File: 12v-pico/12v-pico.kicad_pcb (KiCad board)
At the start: 2 copper layers, 75 x 68 mm, 13 parts, among them J1 MERG 12v CBUS, J2 Adafruit CAN Pal, J3 UART0, J4 DEBUG, J5 Conn_01x20_Pin, J6 Conn_01x20_Pin, SW1 RESET, U1 LM7805_TO220

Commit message: tidied up schematic
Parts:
- renumbered J4 to J3, J3 to J4
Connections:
- net +12V renamed Net-(D1-A)
- SW1 pad 1: Net-(A1-RUN) -> GND
- SW1 pad 2: GND -> Net-(A1-RUN)
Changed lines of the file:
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@@
 	(net 35 "Net-(A1-GPIO0)")
 	(net 36 "Net-(A1-GPIO6)")
-	(net 37 "+12V")
+	(net 37 "Net-(D1-A)")
 	(net 38 "Net-(D1-K)")
 	(net 39 "Net-(D2-A)")
@@
 			(remove_unused_layers no)
 			(net 14 "Net-(A1-VBUS)")
-			(pinfunction "Pin_1")
+			(pinfunction "40")
 			(pintype "passive")
 		)
@@
 		(descr "Through hole straight socket strip, 1x03, 2.54mm pitch, single row (from Kicad 4.0.7), script generated")
 		(tags "Through hole socket strip THT 1x03 2.54mm single row")
-		(property "Reference" "J3"
+		(property "Reference" "J4"
 			(at -3.24 -0.338 0)
 			(layer "F.SilkS")
@@
 			(layers "*.Cu" "*.Mask")
 			(remove_unused_layers no)
-			(net 3 "Net-(A1-RUN)")
+			(net 7 "GND")
 			(pinfunction "1")
 			(pintype "passive")
@@
 			(layers "*.Cu" "*.Mask")
 			(remove_unused_layers no)
-			(net 3 "Net-(A1-RUN)")
+			(net 7 "GND")
 			(pinfunction "1")
 			(pintype "passive")
@@
 			(layers "*.Cu" "*.Mask")
 			(remove_unused_layers no)
-			(net 7 "GND")
+			(net 3 "Net-(A1-RUN)")
 			(pinfunction "2")
 			(pintype "passive")
@@
 			(layers "*.Cu" "*.Mask")
 			(remove_unused_layers no)
-			(net 7 "GND")
+			(net 3 "Net-(A1-RUN)")
 			(pinfunction "2")
 			(pintype "passive")
@@
 			(layers "*.Cu" "*.Mask")
 			(remove_unused_layers no)
-			(net 37 "+12V")
+			(net 37 "Net-(D1-A)")
 			(pinfunction "A")
 			(pintype "passive")
@@
 		(descr "Through hole straight pin header, 1x03, 2.54mm pitch, single row")
 		(tags "Through hole pin header THT 1x03 2.54mm single row")
-		(property "Reference" "J4"
+		(property "Reference" "J3"
 			(at 0 -2.38 90)
 			(layer "F.SilkS")
@@
 			(remove_unused_layers no)
 			(roundrect_rratio 0.104167)
-			(net 37 "+12V")
-			(pinfunction "12v")
+			(net 37 "Net-(D1-A)")
+			(pinfunction "+12v")
 			(pintype "power_out")
 		)

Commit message: design updates
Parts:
- added REF**: MountingHole_3.2mm_M3_Pad, MountingHole:MountingHole_3.2mm_M3_Pad, F.Cu at (213.0, 98.0)
- added REF**: MountingHole_3.2mm_M3_Pad, MountingHole:MountingHole_3.2mm_M3_Pad, F.Cu at (141.0, 98.0)
- added REF**: MountingHole_3.2mm_M3_Pad, MountingHole:MountingHole_3.2mm_M3_Pad, F.Cu at (213.0, 40.0)
- added REF**: MountingHole_3.2mm_M3_Pad, MountingHole:MountingHole_3.2mm_M3_Pad, F.Cu at (141.0, 40.0)
- J5: value Conn_01x20_Pin -> Pico LHS
- J6: value Conn_01x20_Pin -> Pico RHS
- moved D2 29.1 mm to (213.0, 46.9), turned to -90 degrees
- moved D1 26.2 mm to (213.0, 74.1)
- moved C2 26.0 mm to (206.0, 88.5)
- moved U1 25.6 mm to (213.0, 81.0)
- moved C1 24.9 mm to (206.0, 79.0)
- moved J2 14.9 mm to (204.1, 53.0), turned to -90 degrees
- moved J4 10.7 mm to (141.0, 48.0)
- moved SW1 7.27 mm to (177.2, 98.2), turned to 180 degrees
- moved J1 1.74 mm to (201.8, 40.7)
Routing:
- net Net-(A1-GPIO3): track 50.2 -> 73.7 mm
- net Net-(A1-GPIO2): track 50.2 -> 69.7 mm
- net Net-(D1-A): track 8.75 -> 27.9 mm
- net Net-(J1-CANH): track 32.2 -> 13.7 mm
- net Net-(J1-CANL): track 36.2 -> 20.7 mm
- net Net-(A1-3V3): track 22.1 -> 34.1 mm
- net Net-(A1-VSYS): track 17.2 -> 5.55 mm
- net Net-(D2-A): track 48.0 -> 38.2 mm
- net Net-(A1-GPIO1): track 10.6 -> 18.8 mm
- net Net-(A1-GPIO0): track 10.6 -> 18.8 mm
- net Net-(A1-RUN): track 44.0 -> 49.3 mm
- net Net-(A1-GPIO4): track 50.2 -> 51.4 mm
- net Net-(D1-K): track 15.3 -> 14.7 mm
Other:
- board size 75 x 68 mm -> 81.5 x 68 mm

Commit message: complies with design rules
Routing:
- net Net-(A1-VSYS): track 5.55 -> 45.2 mm
- net Net-(A1-GPIO2): track 69.7 -> 70.8 mm
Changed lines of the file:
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@@
 			(at 0 -4.2 0)
 			(layer "F.SilkS")
+			(hide yes)
 			(effects
 				(font
@@
 			(at 0 -4.2 0)
 			(layer "F.SilkS")
+			(hide yes)
 			(effects
 				(font
@@
 			(at 0 -4.2 0)
 			(layer "F.SilkS")
+			(hide yes)
 			(effects
 				(font
@@
 			(at 0 -4.2 0)
 			(layer "F.SilkS")
+			(hide yes)
 			(effects
 				(font
@@
 	)
 	(gr_rect
-		(start 141 40)
-		(end 213 40)
-		(stroke
-			(width 0.1)
-			(type default)
-		)
-		(fill no)
-		(layer "Cmts.User")
-	)
-	(gr_rect
 		(start 136 35)
 		(end 217.5 103)
@@
 	)
 	(segment
-		(start 152.87 44.958)
-		(end 147.32 44.958)
+		(start 200.152 51.848)
+		(end 200.152 39.922665)
 		(width 0.2)
 		(layer "F.Cu")
@@
 	)
 	(segment
-		(start 166.316024 38.489)
-		(end 165.583024 39.222)
+		(start 152.87 44.958)
+		(end 147.32 44.958)
 		(width 0.2)
 		(layer "F.Cu")
@@
 	)
 	(segment
-		(start 200.152 51.848)
-		(end 200.152 39.922665)
+		(start 183.5925 38.4075)
+		(end 178.193 43.807)
 		(width 0.2)
 		(layer "F.Cu")
@@
 	)
 	(segment
-		(start 153.870463 44.958)
-		(end 152.87 44.958)
+		(start 178.193 43.807)
+		(end 162.213018 43.807)
 		(width 0.2)
 		(layer "F.Cu")
@@
 	)
 	(segment
-		(start 182.40324 38.489)
-		(end 166.316024 38.489)
+		(start 199 53)
+		(end 200.152 51.848)
 		(width 0.2)
 		(layer "F.Cu")
@@
 	)
 	(segment
-		(start 159.606463 39.222)
-		(end 153.870463 44.958)
+		(start 198.636835 38.4075)
+		(end 183.5925 38.4075)
 		(width 0.2)
 		(layer "F.Cu")
@@
 	)
 	(segment
-		(start 198.636835 38.4075)
-		(end 182.48474 38.4075)
+		(start 162.213018 43.807)
+		(end 160.922018 42.516)
 		(width 0.2)
 		(layer "F.Cu")
@@
 	)
 	(segment
-		(start 182.48474 38.4075)
-		(end 182.40324 38.489)
+		(start 156.912 42.516)
+		(end 154.47 44.958)
 		(width 0.2)
 		(layer "F.Cu")
@@
 	)
 	(segment
-		(start 200.152 39.922665)
-		(end 198.636835 38.4075)
+		(start 154.47 44.958)
+		(end 152.87 44.958)
 		(width 0.2)
 		(layer "F.Cu")
@@
 	)
 	(segment
-		(start 199 53)
-		(end 200.152 51.848)
+		(start 160.922018 42.516)
+		(end 156.912 42.516)
 		(width 0.2)
 		(layer "F.Cu")
@@
 	)
 	(segment
-		(start 165.583024 39.222)
-		(end 159.606463 39.222)
+		(start 200.152 39.922665)
+		(end 198.636835 38.4075)
 		(width 0.2)
 		(layer "F.Cu")
@@
 	)
 	(segment
+		(start 179.6715 38.0065)
+		(end 177.8 39.878)
+		(width 0.2)
+		(layer "F.Cu")
+		(net 11)
+	)
+	(segment
+		(start 204.0865 38.0065)
+		(end 179.6715 38.0065)
+		(width 0.2)
+		(layer "F.Cu")
+		(net 11)
+	)
+	(segment
+		(start 213 46.92)
+		(end 204.0865 38.0065)
+		(width 0.2)
+		(layer "F.Cu")
+		(net 11)
+	)
+	(segment

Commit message: update symbols and labels
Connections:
- J4 pad 2: Net-(A1-GPIO1) -> GND
- J4 pad 3: GND -> Net-(A1-GPIO1)
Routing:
- net Net-(A1-GPIO1): track 18.8 -> 21.4 mm
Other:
- board text added: "10"
- board text added: "11"
- board text added: "12"
- board text added: "14"
- board text added: "15"
- board text added: "16"
- board text added: "17"
- board text added: "19"
- board text added: "20"
- board text added: "21"
- board text added: "22"
- board text added: "24"
- board text added: "25"
- board text added: "26"
- board text added: "27"
- board text added: "29"
- board text added: "30"
- board text added: "31"
- board text added: "32"
- board text added: "34"
- board text added: "35"
- board text added: "36"
- board text added: "37"
- board text added: "39"
- board text added: "40"
- board text added: "7"
- board text added: "9"
- board text added: "AGND"
- board text added: "GND"
- board text added: "RX"
- board text added: "S"
- board text added: "TX"

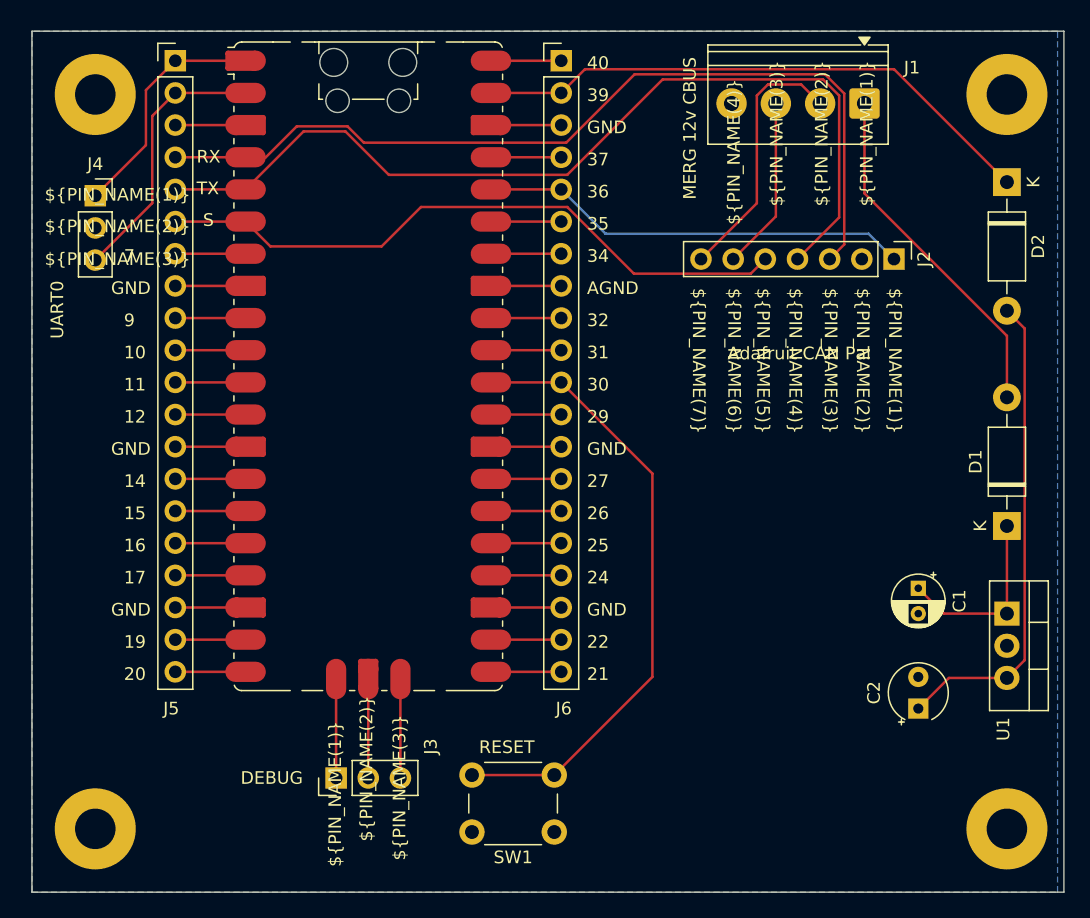
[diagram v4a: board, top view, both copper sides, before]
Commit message: even out board dimensions, label PCB
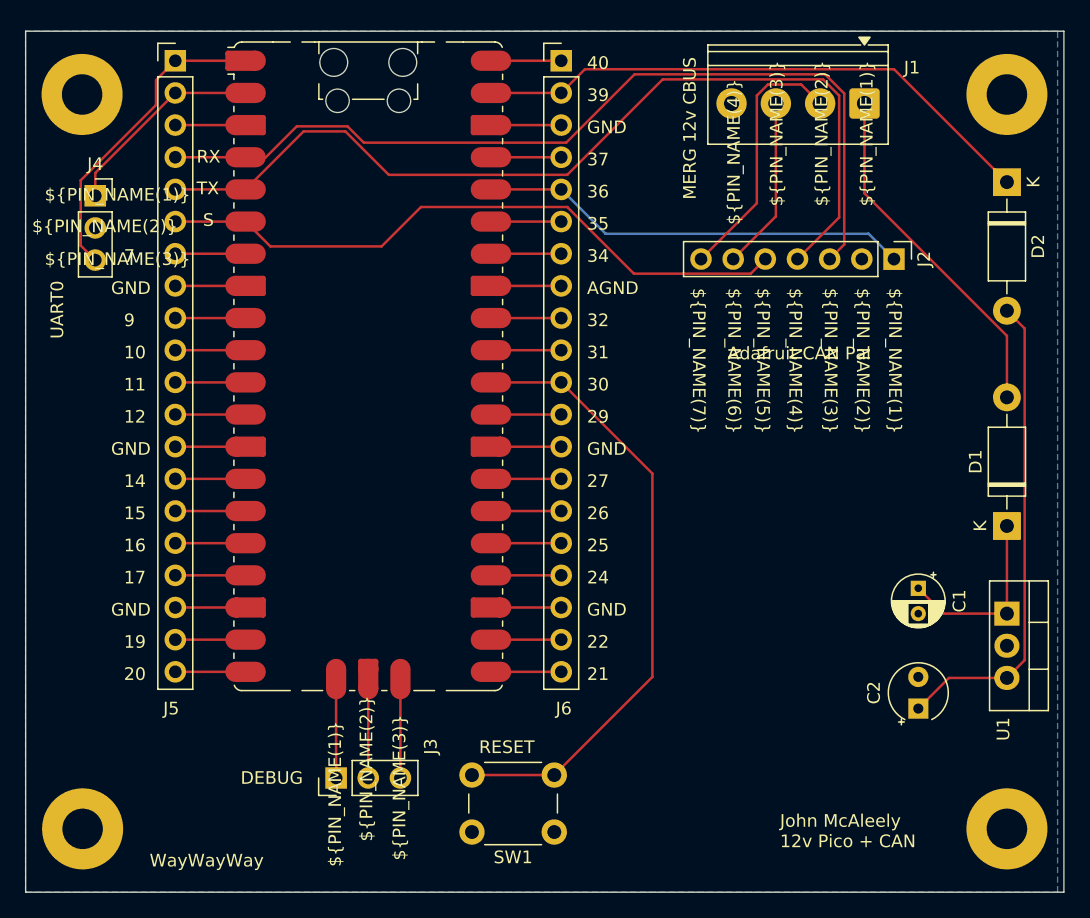
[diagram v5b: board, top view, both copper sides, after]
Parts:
- moved REF** 1.04 mm to (140.0, 40.0)
- moved REF** 1.00 mm to (140.0, 98.0)
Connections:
- J4 pad 1: Net-(A1-GPIO0) -> Net-(A1-GPIO1)
- J4 pad 3: Net-(A1-GPIO1) -> Net-(A1-GPIO0)
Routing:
- net Net-(A1-GPIO0): track 18.8 -> 24.9 mm
- net Net-(A1-GPIO1): track 21.4 -> 16.3 mm
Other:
- board size 81.5 x 68 mm -> 82 x 68 mm
- board text added: "John McAleely 12v Pico + CAN"
- board text added: "WayWayWay"
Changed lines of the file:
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@@
 	(footprint "MountingHole:MountingHole_3.2mm_M3_Pad"
 		(layer "F.Cu")
-		(at 141 98)
+		(at 140 98)
 		(descr "Mounting Hole 3.2mm, M3")
 		(tags "mounting hole 3.2mm m3")
@@
 		)
 		(fp_text user "${PIN_NAME(2)}"
-			(at -4 3 0)
+			(at -5 3 0)
 			(unlocked yes)
 			(layer "F.SilkS")
@@
 			(layers "*.Cu" "*.Mask")
 			(remove_unused_layers no)
-			(net 35 "Net-(A1-GPIO0)")
-			(pinfunction "TX")
-			(pintype "output")
+			(net 17 "Net-(A1-GPIO1)")
+			(pinfunction "RX")
+			(pintype "input")
 		)
 		(pad "2" thru_hole circle
@@
 			(layers "*.Cu" "*.Mask")
 			(remove_unused_layers no)
-			(net 17 "Net-(A1-GPIO1)")
-			(pinfunction "RX")
-			(pintype "input")
+			(net 35 "Net-(A1-GPIO0)")
+			(pinfunction "TX")
+			(pintype "output")
 		)
 		(embedded_fonts no)
@@
 	(footprint "MountingHole:MountingHole_3.2mm_M3_Pad"
 		(layer "F.Cu")
-		(at 141 40)
+		(at 139.96 40)
 		(descr "Mounting Hole 3.2mm, M3")
 		(tags "mounting hole 3.2mm m3")
@@
 	)
 	(gr_rect
-		(start 136 35)
+		(start 135.5 35)
 		(end 217.5 103)
 		(stroke
@@
 		)
 	)
+	(gr_text "John McAleely\n12v Pico + CAN"
+		(at 195.072 99.568 0)
+		(layer "F.SilkS")
+		(effects
+			(font
+				(size 1 1)
+				(thickness 0.1)
+			)
+			(justify left bottom)
+		)
+	)
 	(gr_text "16"
 		(at 143.256 76.2 0)
@@
 		)
 	)
+	(gr_text "WayWayWay"
+		(at 145.288 101.092 0)
+		(layer "F.SilkS")
+		(effects
+			(font
+				(size 1 1)
+				(thickness 0.1)
+			)
+			(justify left bottom)
+		)
+	)
 	(gr_text "14"
 		(at 143.256 71.12 0)
@@
 		)
 	)
+	(dimension
+		(type orthogonal)
+		(layer "Cmts.User")
+		(pts
+			(xy 217.5 103) (xy 135.5 103)
+		)
+		(height 14)
+		(orientation 0)
+		(format
+			(prefix "")
+			(suffix "")
+			(units 3)
+			(units_format 0)
+			(precision 4)
+			(suppress_zeroes yes)
+		)
+		(style
+			(thickness 0.1)
+			(arrow_length 1.27)
+			(text_position_mode 0)
+			(arrow_direction outward)
+			(extension_height 0.58642)
+			(extension_offset 0.5)
+			(keep_text_aligned yes)
+		)
+		(gr_text "82"
+			(at 176.5 115.9 0)
+			(layer "Cmts.User")
+			(effects
+				(font
+					(size 1 1)
+					(thickness 0.1)
+				)
+			)
+		)
+	)
+	(dimension
+		(type orthogonal)
+		(layer "Cmts.User")
+		(pts
+			(xy 140 98) (xy 140 40)
+		)
+		(height -13)
+		(orientation 1)
+		(format
+			(prefix "")
+			(suffix "")
+			(units 3)
+			(units_format 0)
+			(precision 4)
+			(suppress_zeroes yes)
+		)
+		(style
+			(thickness 0.1)
+			(arrow_length 1.27)
+			(text_position_mode 0)
+			(arrow_direction outward)
+			(extension_height 0.58642)
+			(extension_offset 0.5)
+			(keep_text_aligned yes)
+		)
+		(gr_text "58"
+			(at 125.85 69 90)
+			(layer "Cmts.User")
+			(effects
+				(font
+					(size 1 1)
+					(thickness 0.15)
+				)
+			)
+		)
+	)
+	(dimension
+		(type orthogonal)
+		(layer "Cmts.User")
+		(pts
+			(xy 217.5 35) (xy 217.5 103)
+		)
+		(height 15.164)
+		(orientation 1)
+		(format
+			(prefix "")
+			(suffix "")
+			(units 3)
+			(units_format 0)
+			(precision 4)
+			(suppress_zeroes yes)
+		)
+		(style
+			(thickness 0.1)
+			(arrow_length 1.27)
+			(text_position_mode 0)
+			(arrow_direction outward)
+			(extension_height 0.58642)
+			(extension_offset 0.5)
+			(keep_text_aligned yes)
+		)
+		(gr_text "68"
+			(at 231.564 69 90)
+			(layer "Cmts.User")
+			(effects
+				(font
+					(size 1 1)
+					(thickness 0.1)
+				)
+			)
+		)
+	)
+	(dimension
+		(type orthogonal)
+		(layer "Cmts.User")
+		(pts
+			(xy 140 98.08) (xy 213 98)
+		)
+		(height 12.92)
+		(orientation 0)
+		(format
+			(prefix "")
+			(suffix "")
+			(units 3)
+			(units_format 0)
+			(precision 4)
+			(suppress_zeroes yes)
+		)
+		(style
+			(thickness 0.1)
+			(arrow_length 1.27)
+			(text_position_mode 0)
+			(arrow_direction outward)
+			(extension_height 0.58642)
+			(extension_offset 0.5)
+			(keep_text_aligned yes)
+		)
+		(gr_text "73"
+			(at 176.5 109.9 0)
+			(layer "Cmts.User")
+			(effects
+				(font
+					(size 1 1)
+					(thickness 0.1)
+				)
+			)
+		)
+	)
 	(segment
 		(start 172.25 85.598)
@@
 	)
 	(segment
-		(start 145.5 48.58)
-		(end 141 53.08)
+		(start 147.32 39.878)
+		(end 141 46.198)
 		(width 0.2)
 		(layer "F.Cu")
@@
 	)
 	(segment
-		(start 147.32 39.878)
-		(end 145.5 41.698)
+		(start 141 46.198)
+		(end 141 48)
 		(width 0.2)
 		(layer "F.Cu")
@@
 	)
 	(segment
-		(start 145.5 41.698)
-		(end 145.5 48.58)
-		(width 0.2)
-		(layer "F.Cu")
-		(net 17)
-	)
-	(segment
 		(start 147.32 85.598)
 		(end 152.87 85.598)
@@
 	)
 	(segment
+		(start 147.32 37.338)
+		(end 145.796 38.862)
+		(width 0.2)
+		(layer "F.Cu")
+		(net 35)
+	)
+	(segment
+		(start 139.849 51.929)
+		(end 141 53.08)
+		(width 0.2)
+		(layer "F.Cu")
+		(net 35)
+	)
+	(segment
 		(start 152.87 37.338)
 		(end 147.32 37.338)
@@
 	)
 	(segment
-		(start 145 44)
-		(end 141 48)
+		(start 145.796 38.862)
+		(end 145.796 40.8349)
 		(width 0.2)
 		(layer "F.Cu")
@@
 	)
 	(segment
-		(start 147.32 37.338)
-		(end 145 39.658)
+		(start 139.849 46.7819)
+		(end 139.849 51.929)
 		(width 0.2)
 		(layer "F.Cu")
@@
 	)
 	(segment
-		(start 145 39.658)
-		(end 145 44)
+		(start 145.796 40.8349)
+		(end 139.849 46.7819)
 		(width 0.2)
 		(layer "F.Cu")
@@
 		(polygon
 			(pts
-				(xy 217 35) (xy 136 35) (xy 136 103) (xy 217 103)
+				(xy 217 35) (xy 135.492 35) (xy 135.492 103) (xy 217 103)
 			)
 		)
